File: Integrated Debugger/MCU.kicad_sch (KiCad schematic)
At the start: 15 parts, among them SW1 BOOT, U2 STM32F103CBUx, Y1 8MHz

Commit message: Debugger 1.1.2 production files
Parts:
- U2: footprint Picoballoon ICs:QFN-48-1EP_7x7mm_P0.5mm_EP5.6x5.6mm -> Picoballoon ICs:QFN-48 7x7mm
- Y1: footprint Picoballoon Passives:Crystal CSTNE8M00GH5C000R0 -> Picoballoon Passives:Crystal 3213-3P
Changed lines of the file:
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@@
 	(title_block
 		(title "MCU")
-		(date "2025-11-01")
-		(rev "1.1.1")
+		(date "2025-11-03")
+		(rev "1.1.2")
 	)
 	(bus_alias "TARGET_BUS"
@@
 			)
 		)
-		(property "Footprint" "Picoballoon ICs:QFN-48-1EP_7x7mm_P0.5mm_EP5.6x5.6mm"
+		(property "Footprint" "Picoballoon ICs:QFN-48 7x7mm"
 			(at 76.2 101.6 0)
 			(effects
@@
 			)
 		)
-		(property "Footprint" "Picoballoon Passives:Crystal CSTNE8M00GH5C000R0"
+		(property "Footprint" "Picoballoon Passives:Crystal 3213-3P"
 			(at 77.47 40.64 0)
 			(effects

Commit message: IDBG schematic
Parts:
- removed R9: 0Ω, Picoballoon Passives:Resistor 0201, symbol Picoballoon Passives:Resistor
- added C20, C21: 18pF, Picoballoon Passives:Capacitor 0201, symbol Picoballoon Passives:Capacitor
- added FB4: 1000Ω, Picoballoon Passives:Inductor 0402, symbol Picoballoon Passives:Ferrite bead
- added unit 2 of U2
- C1, C17, C2, C3, C4, C5: JLCPCB Part # C76934 -> (none)
- C6: JLCPCB Part # C76930 -> (none)
- C7: JLCPCB Part # C335103 -> (none)
- R10, R12: JLCPCB Part # C717002 -> (none)
- R11: JLCPCB Part # C138135 -> (none)
- U2: JLCPCB Part # C55506 -> (none)
- Y1: footprint Picoballoon Passives:Crystal 3213-3P -> Picoballoon Passives:Crystal 3225; JLCPCB Part # C341525 -> (none); LCSC Part # C341525 -> C57131; MPN CSTNE8M00GH5C000R0 -> 1C208000BC0R
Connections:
- net GND: now also C20.1, C21.1, U2.23 (VSS), U2.35 (VSS), U2.47 (VSS), U2.49 (VSS), U2.8 (VSSA); no longer U2.23 (VSS), U2.35 (VSS), U2.47 (VSS), U2.49 (VSS), U2.8 (VSSA)
- net i.TDO: now also U2.43 (PB7)
- net at Y1.3: now also C21.2, U2.6 (PD1); no longer U2.5 (PD0)
- net at Y1.1: now also C20.2, U2.5 (PD0); no longer U2.6 (PD1)
- removed net +3.3V: C2.2, C3.2, C4.2, C5.2, C6.2, C7.2, R10.1, U2.1 (VBAT), U2.24 (VDD), U2.36 (VDD), U2.40 (PB4), U2.41 (PB5), U2.42 (PB6), U2.48 (VDD), U2.9 (VDDA)
- net TRACESWO: no longer names the net of U2.39 (PB3)
- net V_TARGET renamed VDD_TG
- new net: C2.2, C3.2, C4.2, C5.2, C6.2, C7.2, FB4.2, U2.1 (VBAT), U2.24 (VDD), U2.36 (VDD), U2.48 (VDD), U2.9 (VDDA)
- new net VDD_3V3: FB4.1, R10.1, U2.40 (PB4), U2.41 (PB5), U2.42 (PB6)
- no-connect marks 8 -> 9
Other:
- note added: "MCU DIGITAL I/O"
- note added: "MCU POWER & CLOCKS"
- note removed: "MCU DECOUPLING"
- moved on the sheet: C1, C17, C2, C3, C4, C5, C6, C7, R10, R11, R12, SW1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

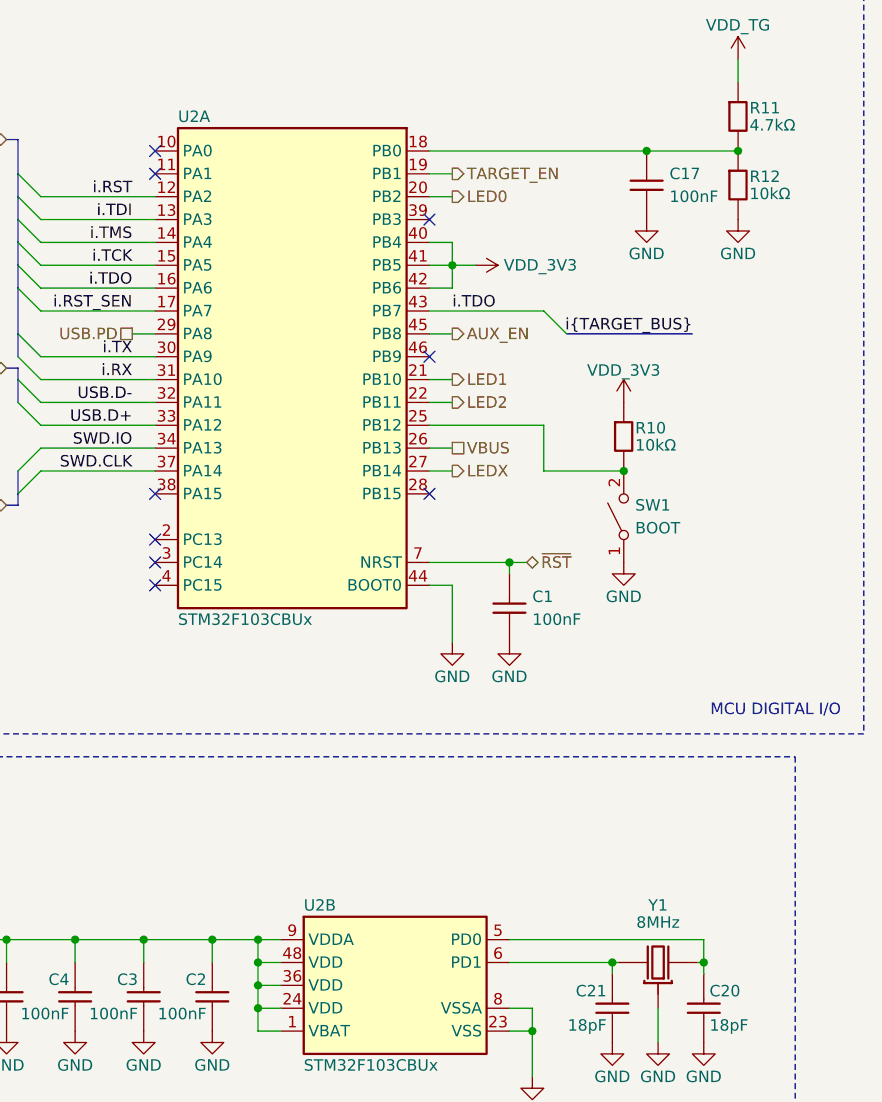
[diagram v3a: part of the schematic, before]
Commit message: Integrated debugger PCB
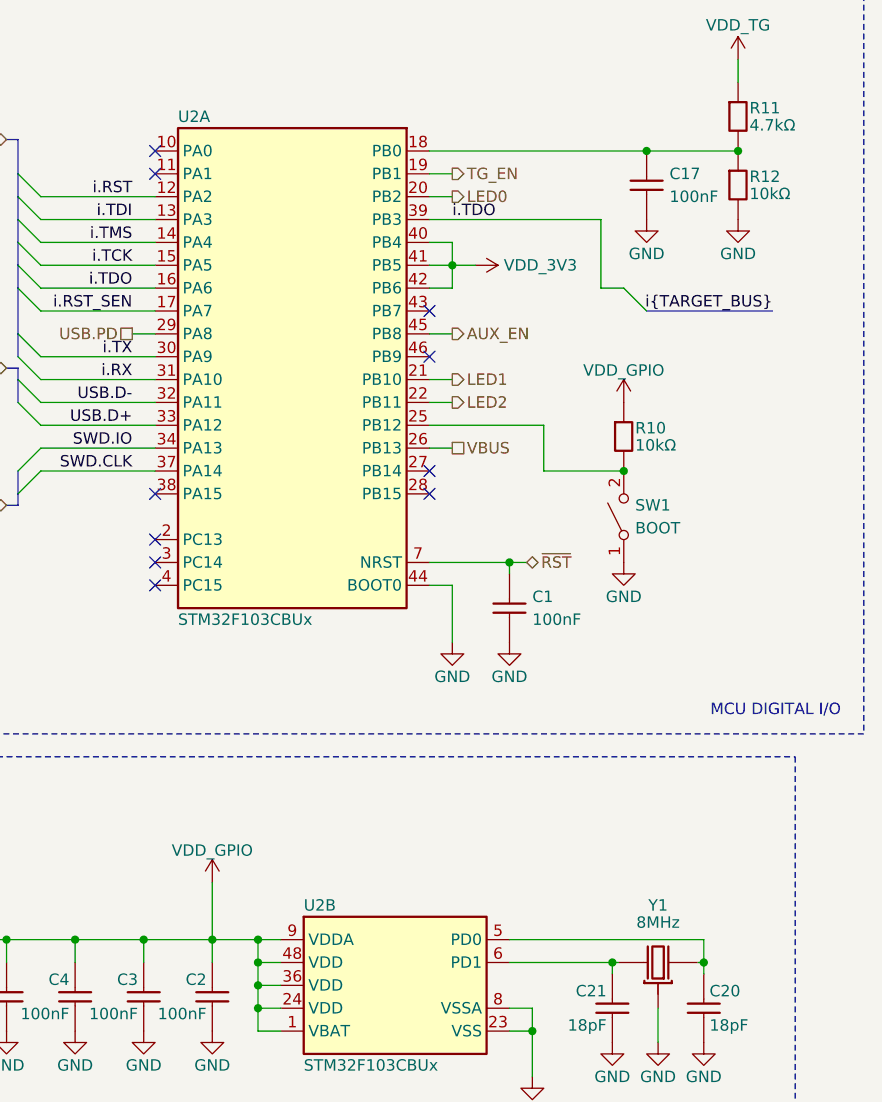
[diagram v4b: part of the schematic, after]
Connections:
- net GND: now also Y1.4
- net VDD_3V3: no longer R10.1
- net i.TDO: now also U2.39 (PB3); no longer U2.43 (PB7)
- net VDD_GPIO: now reaches C2.2, C3.2, C4.2, C5.2, C6.2, C7.2, FB4.2, U2.1 (VBAT), U2.24 (VDD), U2.36 (VDD), U2.48 (VDD), U2.9 (VDDA)
- net VDD_GPIO: now also R10.1
- net LEDX: no longer names the net of U2.27 (PB14)
- net TARGET_EN renamed TG_EN
- no-connect marks 9 -> 10
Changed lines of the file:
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@@
 	)
 	(no_connect
-		(at 78.74 34.29)
+		(at 78.74 44.45)
 	)
 	(no_connect
@@
 	)
 	(no_connect
+		(at 78.74 62.23)
+	)
+	(no_connect
 		(at 78.74 64.77)
 	)
 	(bus_entry
-		(at 91.44 44.45)
+		(at 100.33 41.91)
 		(size 2.54 2.54)
 		(stroke
@@
 	(wire
 		(pts
+			(xy 78.74 34.29) (xy 97.79 34.29)
+		)
+		(stroke
+			(width 0)
+			(type default)
+		)
+	)
+	(wire
+		(pts
 			(xy 59.69 114.3) (xy 62.23 114.3)
 		)
@@
 	(wire
 		(pts
+			(xy 97.79 41.91) (xy 100.33 41.91)
+		)
+		(stroke
+			(width 0)
+			(type default)
+		)
+	)
+	(wire
+		(pts
 			(xy 91.44 57.15) (xy 78.74 57.15)
 		)
@@
 		)
 	)
-	(bus
+	(wire
 		(pts
-			(xy 33.02 41.91) (xy 33.02 39.37)
+			(xy 97.79 34.29) (xy 97.79 41.91)
 		)
 		(stroke
@@
 		)
 	)
-	(wire
+	(bus
 		(pts
-			(xy 81.28 62.23) (xy 78.74 62.23)
+			(xy 33.02 41.91) (xy 33.02 39.37)
 		)
 		(stroke
@@
 	(wire
 		(pts
+			(xy 54.61 107.95) (xy 54.61 114.3)
+		)
+		(stroke
+			(width 0)
+			(type default)
+		)
+	)
+	(wire
+		(pts
 			(xy 102.87 26.67) (xy 113.03 26.67)
 		)
@@
 	(bus
 		(pts
-			(xy 107.95 46.99) (xy 93.98 46.99)
-		)
-		(stroke
-			(width 0)
-			(type default)
-		)
-	)
-	(wire
-		(pts
-			(xy 78.74 44.45) (xy 91.44 44.45)
+			(xy 116.84 44.45) (xy 102.87 44.45)
 		)
 		(stroke
@@
 	)
 	(label "i{TARGET_BUS}"
-		(at 107.95 46.99 180)
+		(at 116.84 44.45 180)
 		(effects
 			(font
@@
 	)
 	(label "i.TDO"
-		(at 81.28 44.45 0)
+		(at 81.28 34.29 0)
 		(effects
 			(font
@@
 		)
 	)
-	(hierarchical_label "LEDX"
-		(shape output)
-		(at 81.28 62.23 0)
-		(effects
-			(font
-				(size 1.27 1.27)
-			)
-			(justify left)
-		)
-	)
 	(hierarchical_label "SWD{IO CLK}"
 		(shape bidirectional)
@@
 		)
 	)
-	(hierarchical_label "TARGET_EN"
+	(hierarchical_label "TG_EN"
 		(shape output)
 		(at 81.28 29.21 0)
@@
 	)
 	(symbol
-		(lib_id "Picoballoon Passives:Capacitor")
-		(at 109.22 121.92 180)
+		(lib_id "Picoballoon Power Symbols:+3.3V")
+		(at 100.33 54.61 0)
 		(unit 1)
 		(exclude_from_sim no)
@@
 		(on_board yes)
 		(dnp no)
-		(property "Reference" "C20"
-			(at 109.855 120.015 0)
-			(effects
-				(font
-					(size 1.27 1.27)
-				)
-				(justify right)
-			)
-		)
-		(property "Value" "18pF"
-			(at 109.855 123.825 0)
-			(effects
-				(font
-					(size 1.27 1.27)
-				)
-				(justify right)
-			)
-		)
-		(property "Footprint" "Picoballoon Passives:Capacitor 0201"
-			(at 109.22 111.125 0)
+		(fields_autoplaced yes)
+		(property "Reference" "#PWR091"
+			(at 100.33 58.42 0)
 			(effects
 				(font
@@
 			)
 		)
-		(property "Datasheet" "https://jlcpcb.com/api/file/downloadByFileSystemAccessId/8588903659258458112"
-			(at 109.22 121.92 0)
+		(property "Value" "VDD_GPIO"
+			(at 100.33 51.054 0)
+			(do_not_autoplace yes)
 			(effects
 				(font
 					(size 1.27 1.27)
 				)
-				(hide yes)
 			)
 		)
-		(property "Description" "Generic MLCC"
-			(at 109.22 121.92 0)
+		(property "Footprint" ""
+			(at 100.33 54.61 0)
 			(effects
 				(font
@@
 			)
 		)
-		(property "MPN" "GRM0335C1H180GA01D"
-			(at 109.22 121.92 0)
+		(property "Datasheet" ""
+			(at 100.33 54.61 0)
 			(effects
 				(font
@@
 			)
 		)
-		(property "LCSC Part #" "C161409"
-			(at 109.22 121.92 0)
+		(property "Description" "Power symbol creates a global label with name \"+3.3V\""
+			(at 100.33 54.61 0)
 			(effects
 				(font
@@
 		(pin "1"
 		)
-		(pin "2"
-		)
 		(instances
 			(project "Integrated Debugger"
 				(path "/ce538ebe-fda9-4af3-9f8c-9fd5bf58f0e4/b916d44a-03d1-4a04-a023-19b38caca2ea"
-					(reference "C20")
+					(reference "#PWR091")
 					(unit 1)
 				)
@@
 	)
 	(symbol
-		(lib_id "Picoballoon Power Symbols:+3.3V")
-		(at 83.82 39.37 270)
+		(lib_id "Picoballoon Passives:Capacitor")
+		(at 109.22 121.92 180)
 		(unit 1)
 		(exclude_from_sim no)
@@
 		(on_board yes)
 		(dnp no)
-		(property "Reference" "#PWR09"
-			(at 80.01 39.37 0)
+		(property "Reference" "C20"
+			(at 109.855 120.015 0)
+			(effects
+				(font
+					(size 1.27 1.27)
+				)
+				(justify right)
+			)
+		)
+		(property "Value" "18pF"
+			(at 109.855 123.825 0)
+			(effects
+				(font
+					(size 1.27 1.27)
+				)
+				(justify right)
+			)
+		)
+		(property "Footprint" "Picoballoon Passives:Capacitor 0201"
+			(at 109.22 111.125 0)
 			(effects
 				(font
@@
 			)
 		)
-		(property "Value" "VDD_3V3"
-			(at 86.995 39.37 90)
-			(do_not_autoplace yes)
+		(property "Datasheet" "https://jlcpcb.com/api/file/downloadByFileSystemAccessId/8588903659258458112"
+			(at 109.22 121.92 0)
 			(effects
 				(font
 					(size 1.27 1.27)
 				)
-				(justify left)
+				(hide yes)
 			)
 		)
-		(property "Footprint" ""
-			(at 83.82 39.37 0)
+		(property "Description" "Generic MLCC"
+			(at 109.22 121.92 0)
 			(effects
 				(font
@@
 			)
 		)
-		(property "Datasheet" ""
-			(at 83.82 39.37 0)
+		(property "MPN" "GRM0335C1H180GA01D"
+			(at 109.22 121.92 0)
 			(effects
 				(font
@@
 			)
 		)
-		(property "Description" "Power symbol creates a global label with name \"+3.3V\""
-			(at 83.82 39.37 0)
+		(property "LCSC Part #" "C161409"
+			(at 109.22 121.92 0)
 			(effects
 				(font
@@
 		(pin "1"
 		)
+		(pin "2"
+		)
 		(instances
 			(project "Integrated Debugger"
 				(path "/ce538ebe-fda9-4af3-9f8c-9fd5bf58f0e4/b916d44a-03d1-4a04-a023-19b38caca2ea"
-					(reference "#PWR09")
+					(reference "C20")
 					(unit 1)
 				)
@@
 	(symbol
 		(lib_id "Picoballoon Power Symbols:+3.3V")
-		(at 100.33 54.61 0)
+		(at 83.82 39.37 270)
 		(unit 1)
 		(exclude_from_sim no)
@@
 		(on_board yes)
 		(dnp no)
-		(fields_autoplaced yes)
-		(property "Reference" "#PWR070"
-			(at 100.33 58.42 0)
+		(property "Reference" "#PWR09"
+			(at 80.01 39.37 0)
 			(effects
 				(font
@@
 		)
 		(property "Value" "VDD_3V3"
-			(at 100.33 51.054 0)
+			(at 86.995 39.37 90)
 			(do_not_autoplace yes)
 			(effects
@@
 					(size 1.27 1.27)
 				)
+				(justify left)
 			)
 		)
 		(property "Footprint" ""
-			(at 100.33 54.61 0)
+			(at 83.82 39.37 0)
 			(effects
 				(font
@@
 		)
 		(property "Datasheet" ""
-			(at 100.33 54.61 0)
+			(at 83.82 39.37 0)
 			(effects
 				(font
@@
 		)
 		(property "Description" "Power symbol creates a global label with name \"+3.3V\""
-			(at 100.33 54.61 0)
+			(at 83.82 39.37 0)
 			(effects
 				(font
@@
 			(project "Integrated Debugger"
 				(path "/ce538ebe-fda9-4af3-9f8c-9fd5bf58f0e4/b916d44a-03d1-4a04-a023-19b38caca2ea"
-					(reference "#PWR070")
+					(reference "#PWR09")
 					(unit 1)
 				)
@@
 	)
 	(symbol
+		(lib_id "Picoballoon Power Symbols:+3.3V")
+		(at 54.61 107.95 0)
+		(unit 1)
+		(exclude_from_sim no)
+		(in_bom yes)
+		(on_board yes)
+		(dnp no)
+		(fields_autoplaced yes)
+		(property "Reference" "#PWR090"
+			(at 54.61 111.76 0)
+			(effects
+				(font
+					(size 1.27 1.27)
+				)
+				(hide yes)
+			)
+		)
+		(property "Value" "VDD_GPIO"
+			(at 54.61 104.394 0)
+			(do_not_autoplace yes)
+			(effects
+				(font
+					(size 1.27 1.27)
+				)
+			)
+		)
+		(property "Footprint" ""
+			(at 54.61 107.95 0)
+			(effects
+				(font
+					(size 1.27 1.27)
+				)
+				(hide yes)
+			)
+		)
+		(property "Datasheet" ""
+			(at 54.61 107.95 0)
+			(effects
+				(font
+					(size 1.27 1.27)
+				)
+				(hide yes)
+			)
+		)
+		(property "Description" "Power symbol creates a global label with name \"+3.3V\""
+			(at 54.61 107.95 0)
+			(effects
+				(font
+					(size 1.27 1.27)
+				)
+				(hide yes)
+			)
+		)
+		(pin "1"
+		)
+		(instances
+			(project "Integrated Debugger"
+				(path "/ce538ebe-fda9-4af3-9f8c-9fd5bf58f0e4/b916d44a-03d1-4a04-a023-19b38caca2ea"
+					(reference "#PWR090")
+					(unit 1)
+				)
+			)
+		)
+	)
+	(symbol
 		(lib_id "Picoballoon Passives:Capacitor")
 		(at 16.51 120.65 0)
@@
 		(pin "2"
 		)
+		(pin "4"
+		)
+		(pin "4"
+		)
 		(instances

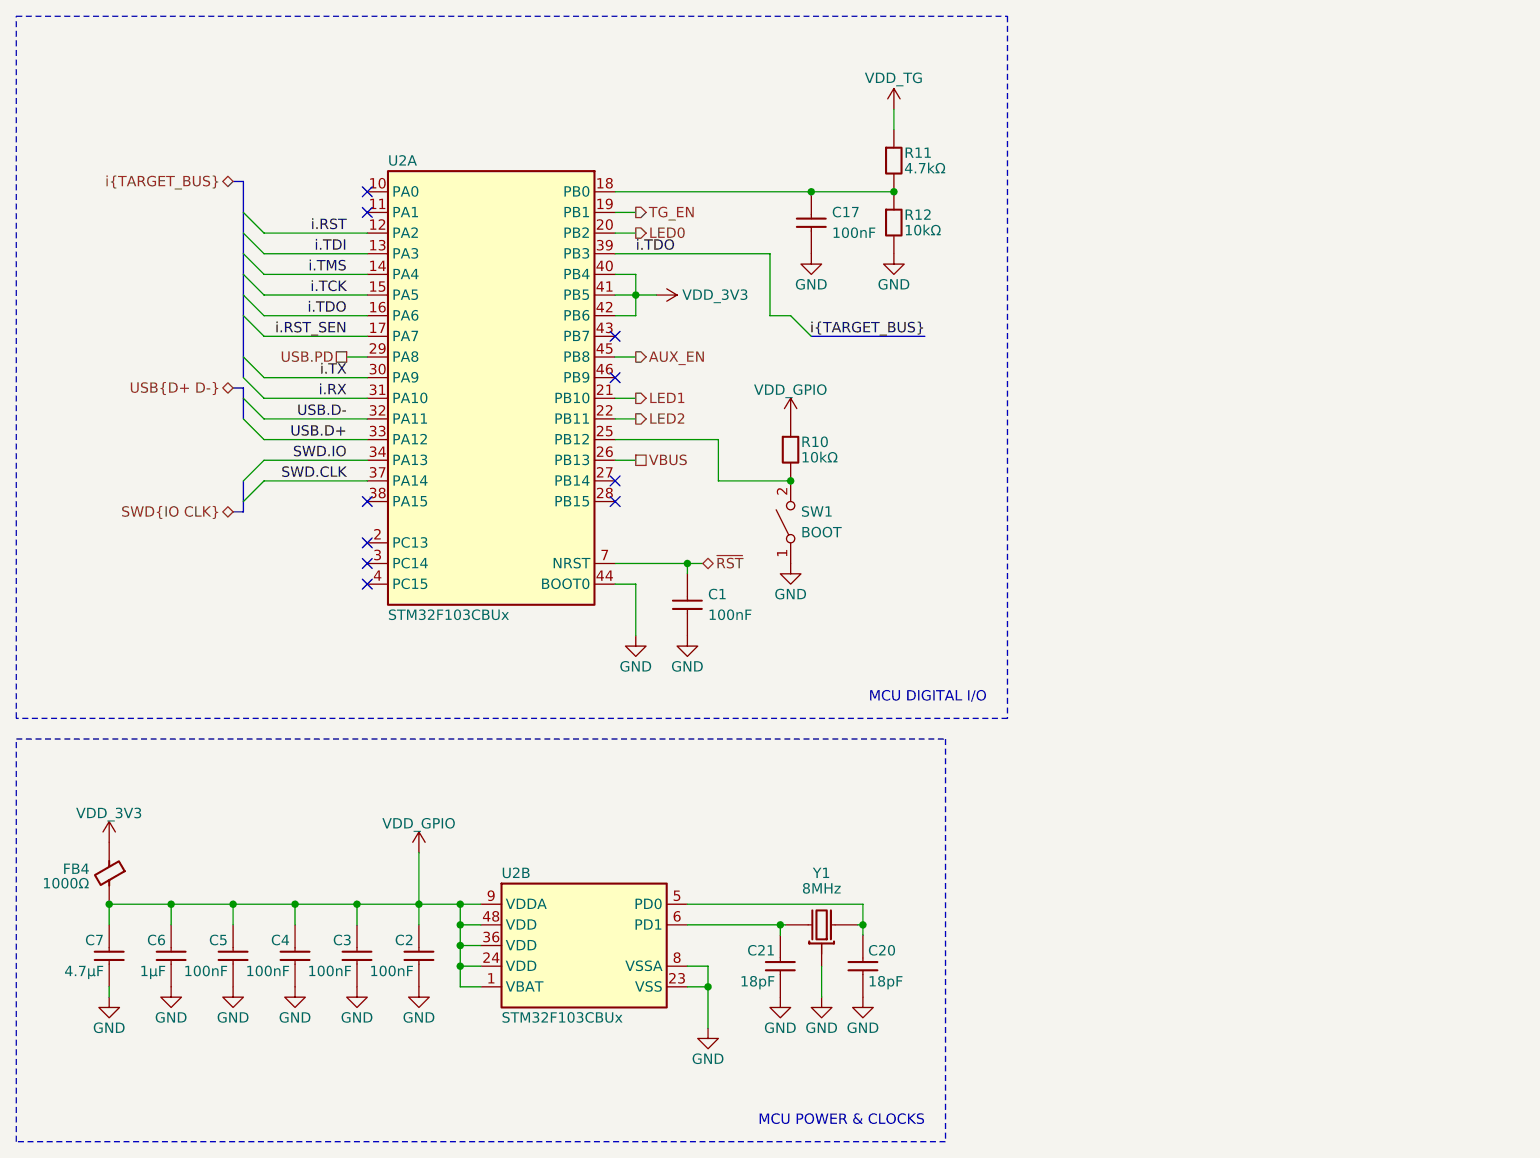
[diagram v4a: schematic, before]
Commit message: Reannotate schematic, update GND plane
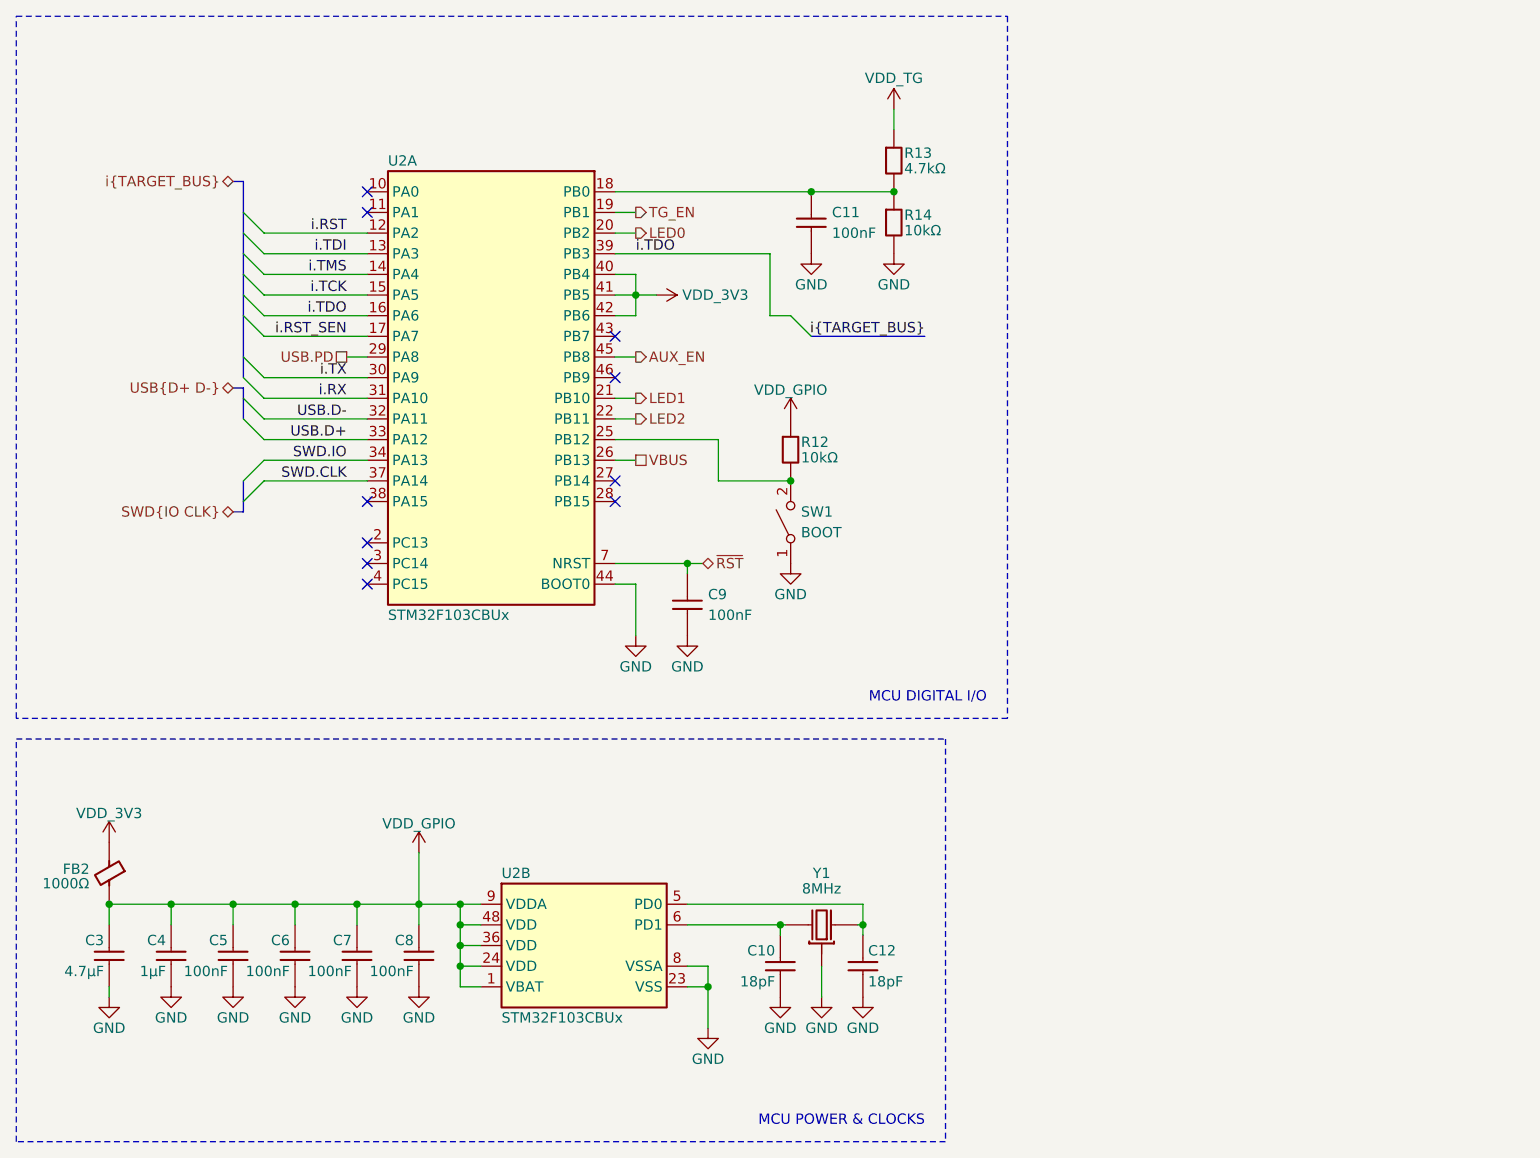
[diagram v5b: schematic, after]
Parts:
- renumbered C21 to C10, C17 to C11, C20 to C12, C7 to C3, C6 to C4, C4 to C6, C3 to C7, C2 to C8, C1 to C9, FB4 to FB2, R10 to R12, R11 to R13, R12 to R14
